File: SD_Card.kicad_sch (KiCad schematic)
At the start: 1 part, among them J8 Micro_SD_Card_Det1

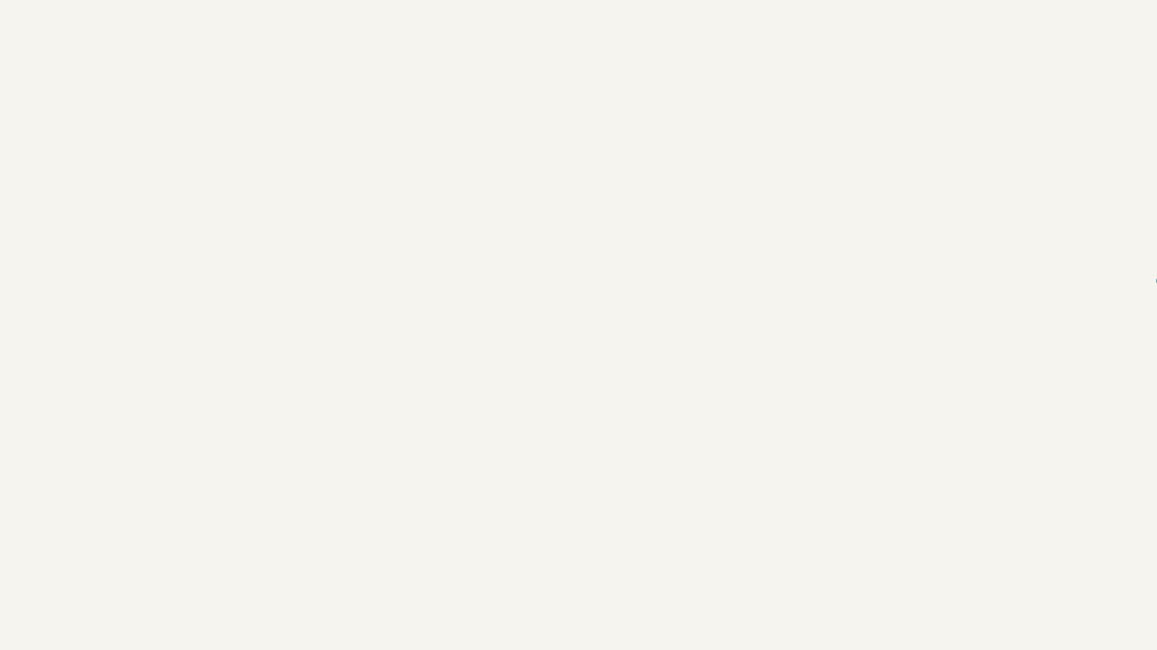
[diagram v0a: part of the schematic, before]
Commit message: Added SD card protection
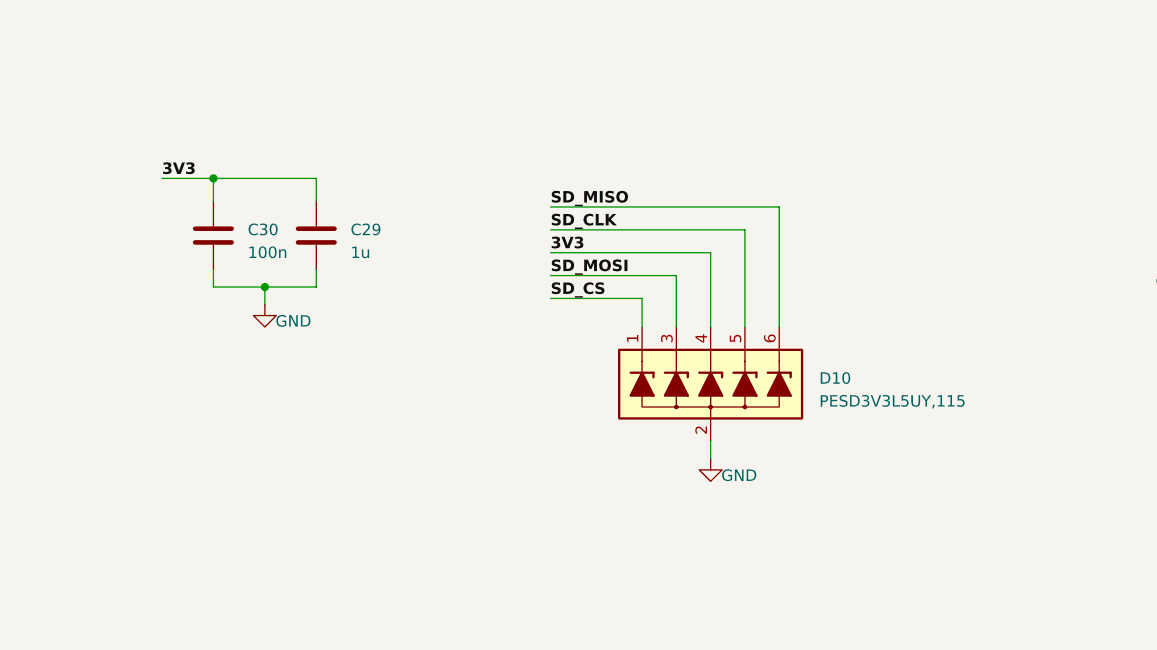
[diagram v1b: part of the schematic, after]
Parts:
- added C29: 1u, symbol ESP32-S3_DB:C
- added C30: 100n, symbol ESP32-S3_DB:C
- added D10: PESD3V3L5UY,115, Package_TO_SOT_SMD_AKL:SOT-363_SC-70-6, symbol ESP32-S3_DB:PESD3V3L5UY
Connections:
- net 3V3: now also C29.1, C30.1, D10.4 (L3)
- net GND: now also C29.2, C30.2, D10.2 (VN)
- net SD_CLK: now also D10.5 (L4)
- net SD_CS: now also D10.1 (L1)
- net SD_MISO: now also D10.6 (L5)
- net SD_MOSI: now also D10.3 (L2)
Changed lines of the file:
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@@
 (kicad_sch (version 20230121) (generator eeschema)
   (paper "A4")
+  (junction (at 80.645 70.485) (diameter 0) (color 0 0 0 0)
+  )
+  (junction (at 74.93 58.42) (diameter 0) (color 0 0 0 0)
+  )
   (no_connect (at 196.85 70.485))
   (no_connect (at 240.03 75.565))
@@
     (stroke (width 0) (type default))
   )
+  (wire (pts (xy 74.93 70.485) (xy 80.645 70.485))
+    (stroke (width 0) (type default))
+  )
   (wire (pts (xy 40.64 164.465) (xy 29.21 164.465))
     (stroke (width 0) (type default))
   )
+  (wire (pts (xy 112.395 69.215) (xy 126.365 69.215))
+    (stroke (width 0) (type default))
+  )
+  (wire (pts (xy 74.93 58.42) (xy 86.36 58.42))
+    (stroke (width 0) (type default))
+  )
+  (wire (pts (xy 86.36 70.485) (xy 86.36 68.58))
+    (stroke (width 0) (type default))
+  )
   (wire (pts (xy 40.64 167.005) (xy 29.21 167.005))
     (stroke (width 0) (type default))
   )
+  (wire (pts (xy 74.93 68.58) (xy 74.93 70.485))
+    (stroke (width 0) (type default))
+  )
   (wire (pts (xy 40.64 169.545) (xy 29.21 169.545))
     (stroke (width 0) (type default))
   )
+  (wire (pts (xy 130.175 66.675) (xy 130.175 74.93))
+    (stroke (width 0) (type default))
+  )
+  (wire (pts (xy 137.795 61.595) (xy 137.795 74.93))
+    (stroke (width 0) (type default))
+  )
   (wire (pts (xy 181.61 65.405) (xy 196.85 65.405))
     (stroke (width 0) (type default))
   )
+  (wire (pts (xy 74.93 60.96) (xy 74.93 58.42))
+    (stroke (width 0) (type default))
+  )
   (wire (pts (xy 184.15 55.245) (xy 196.85 55.245))
     (stroke (width 0) (type default))
   )
+  (wire (pts (xy 126.365 69.215) (xy 126.365 74.93))
+    (stroke (width 0) (type default))
+  )
+  (wire (pts (xy 80.645 70.485) (xy 86.36 70.485))
+    (stroke (width 0) (type default))
+  )
+  (wire (pts (xy 112.395 71.755) (xy 122.555 71.755))
+    (stroke (width 0) (type default))
+  )
+  (wire (pts (xy 80.645 70.485) (xy 80.645 72.39))
+    (stroke (width 0) (type default))
+  )
+  (wire (pts (xy 130.175 89.535) (xy 130.175 87.63))
+    (stroke (width 0) (type default))
+  )
+  (wire (pts (xy 112.395 66.675) (xy 130.175 66.675))
+    (stroke (width 0) (type default))
+  )
+  (wire (pts (xy 122.555 71.755) (xy 122.555 74.93))
+    (stroke (width 0) (type default))
+  )
   (wire (pts (xy 184.15 57.785) (xy 196.85 57.785))
     (stroke (width 0) (type default))
   )
+  (wire (pts (xy 112.395 64.135) (xy 133.985 64.135))
+    (stroke (width 0) (type default))
+  )
   (wire (pts (xy 184.15 62.865) (xy 196.85 62.865))
     (stroke (width 0) (type default))
   )
+  (wire (pts (xy 86.36 58.42) (xy 86.36 60.96))
+    (stroke (width 0) (type default))
+  )
+  (wire (pts (xy 112.395 61.595) (xy 137.795 61.595))
+    (stroke (width 0) (type default))
+  )
   (wire (pts (xy 40.64 174.625) (xy 29.21 174.625))
     (stroke (width 0) (type default))
   )
+  (wire (pts (xy 69.215 58.42) (xy 74.93 58.42))
+    (stroke (width 0) (type default))
+  )
   (wire (pts (xy 184.15 60.325) (xy 196.85 60.325))
     (stroke (width 0) (type default))
@@
     (stroke (width 0) (type default))
   )
+  (wire (pts (xy 133.985 64.135) (xy 133.985 74.93))
+    (stroke (width 0) (type default))
+  )
   (label "SD_CS" (at 184.15 55.245 0) (fields_autoplaced)
     (effects (font (size 1.27 1.27) bold (color 204 102 0 1)) (justify left bottom))
   )
+  (label "SD_CS" (at 112.395 71.755 0) (fields_autoplaced)
+    (effects (font (size 1.27 1.27) bold (color 204 102 0 1)) (justify left bottom))
+  )
   (label "SD_CLK" (at 40.64 169.545 0) (fields_autoplaced)
     (effects (font (size 1.27 1.27) bold (color 204 102 0 1)) (justify left bottom))
@@
     (effects (font (size 1.27 1.27) bold (color 204 102 0 1)) (justify left bottom))
   )
+  (label "3V3" (at 112.395 66.675 0) (fields_autoplaced)
+    (effects (font (size 1.27 1.27) bold (color 255 0 0 1)) (justify left bottom))
+  )
   (label "SD_MOSI" (at 184.15 57.785 0) (fields_autoplaced)
+    (effects (font (size 1.27 1.27) bold (color 204 102 0 1)) (justify left bottom))
+  )
+  (label "SD_MOSI" (at 112.395 69.215 0) (fields_autoplaced)
     (effects (font (size 1.27 1.27) bold (color 204 102 0 1)) (justify left bottom))
   )
@@
     (effects (font (size 1.27 1.27) bold (color 255 0 0 1)) (justify left bottom))
   )
+  (label "SD_MISO" (at 112.395 61.595 0) (fields_autoplaced)
+    (effects (font (size 1.27 1.27) bold (color 204 102 0 1)) (justify left bottom))
+  )
   (label "3V3" (at 184.15 60.325 0) (fields_autoplaced)
     (effects (font (size 1.27 1.27) bold (color 255 0 0 1)) (justify left bottom))
@@
   (label "SD_CS" (at 40.64 167.005 0) (fields_autoplaced)
     (effects (font (size 1.27 1.27) bold (color 204 102 0 1)) (justify left bottom))
+  )
+  (label "SD_CLK" (at 112.395 64.135 0) (fields_autoplaced)
+    (effects (font (size 1.27 1.27) bold (color 204 102 0 1)) (justify left bottom))
+  )
+  (label "3V3" (at 69.215 58.42 0) (fields_autoplaced)
+    (effects (font (size 1.27 1.27) bold (color 255 0 0 1)) (justify left bottom))
   )
   (label "SD_CLK" (at 184.15 62.865 0) (fields_autoplaced)
@@
         )
       )
+    )
+  )
+  (symbol (lib_id "ESP32-S3_DB:GND") (at 130.175 89.535 0) (unit 1)
+    (in_bom yes) (on_board yes) (dnp no)
+    (property "Reference" "#PWR055" (at 130.175 95.885 0)
+      (effects (font (size 1.27 1.27)) hide)
+    )
+    (property "Value" "GND" (at 133.35 91.44 0)
+      (effects (font (size 1.27 1.27)))
+    )
+    (property "Footprint" "" (at 130.175 89.535 0)
+      (effects (font (size 1.27 1.27)) hide)
+    )
+    (property "Datasheet" "" (at 130.175 89.535 0)
+      (effects (font (size 1.27 1.27)) hide)
+    )
+    (pin "1")
+    (instances
+      (project "ESP32-S3_DB"
+        (path "/b7fc4bd3-c219-4455-832b-8d795385dcf1/3994ddb3-4428-4f96-b9f4-a7790f668af6"
+          (reference "#PWR055") (unit 1)
+        )
+      )
+    )
+  )
+  (symbol (lib_id "ESP32-S3_DB:GND") (at 80.645 72.39 0) (unit 1)
+    (in_bom yes) (on_board yes) (dnp no)
+    (property "Reference" "#PWR056" (at 80.645 78.74 0)
+      (effects (font (size 1.27 1.27)) hide)
+    )
+    (property "Value" "GND" (at 83.82 74.295 0)
+      (effects (font (size 1.27 1.27)))
+    )
+    (property "Footprint" "" (at 80.645 72.39 0)
+      (effects (font (size 1.27 1.27)) hide)
+    )
+    (property "Datasheet" "" (at 80.645 72.39 0)
+      (effects (font (size 1.27 1.27)) hide)
+    )
+    (pin "1")
+    (instances
+      (project "ESP32-S3_DB"
+        (path "/b7fc4bd3-c219-4455-832b-8d795385dcf1/3994ddb3-4428-4f96-b9f4-a7790f668af6"
+          (reference "#PWR056") (unit 1)
+        )
+      )
+    )
+  )
+  (symbol (lib_id "ESP32-S3_DB:C") (at 74.93 64.77 0) (unit 1)
+    (in_bom yes) (on_board yes) (dnp no) (fields_autoplaced)
+    (property "Reference" "C30" (at 78.74 64.135 0)
+      (effects (font (size 1.27 1.27)) (justify left))
+    )
+    (property "Value" "100n" (at 78.74 66.675 0)
+      (effects (font (size 1.27 1.27)) (justify left))
+    )
+    (property "Footprint" "" (at 75.8952 68.58 0)
+      (effects (font (size 1.27 1.27)) hide)
+    )
+    (property "Datasheet" "~" (at 74.93 64.77 0)
+      (effects (font (size 1.27 1.27)) hide)
+    )
+    (pin "1")
+    (pin "2")
+    (instances
+      (project "ESP32-S3_DB"
+        (path "/b7fc4bd3-c219-4455-832b-8d795385dcf1/3994ddb3-4428-4f96-b9f4-a7790f668af6"
+          (reference "C30") (unit 1)
+        )
+      )
+    )
+  )
+  (symbol (lib_id "ESP32-S3_DB:C") (at 86.36 64.77 0) (unit 1)
+    (in_bom yes) (on_board yes) (dnp no) (fields_autoplaced)
+    (property "Reference" "C29" (at 90.17 64.135 0)
+      (effects (font (size 1.27 1.27)) (justify left))
+    )
+    (property "Value" "1u" (at 90.17 66.675 0)
+      (effects (font (size 1.27 1.27)) (justify left))
+    )
+    (property "Footprint" "" (at 87.3252 68.58 0)
+      (effects (font (size 1.27 1.27)) hide)
+    )
+    (property "Datasheet" "~" (at 86.36 64.77 0)
+      (effects (font (size 1.27 1.27)) hide)
+    )
+    (pin "1")
+    (pin "2")
+    (instances
+      (project "ESP32-S3_DB"
+        (path "/b7fc4bd3-c219-4455-832b-8d795385dcf1/3994ddb3-4428-4f96-b9f4-a7790f668af6"
+          (reference "C29") (unit 1)
+        )
+      )
+    )
+  )
+  (symbol (lib_id "ESP32-S3_DB:PESD3V3L5UY") (at 130.175 81.28 0) (unit 1)
+    (in_bom yes) (on_board yes) (dnp no) (fields_autoplaced)
+    (property "Reference" "D10" (at 142.24 80.645 0)
+      (effects (font (size 1.27 1.27)) (justify left))
+    )
+    (property "Value" "PESD3V3L5UY,115" (at 142.24 83.185 0)
+      (effects (font (size 1.27 1.27)) (justify left))
+    )
+    (property "Footprint" "Package_TO_SOT_SMD_AKL:SOT-363_SC-70-6" (at 130.175 81.28 0)
+      (effects (font (size 1.27 1.27)) hide)
+    )
+    (property "Datasheet" "https://www.tme.eu/Document/d7b061109274755b8c3532aab9d13eb5/PESD5V0L5UV-DTE.pdf" (at 130.175 81.28 0)
+      (effects (font (size 1.27 1.27)) hide)
+    )
+    (pin "1")
+    (pin "2")
+    (pin "3")
+    (pin "4")
+    (pin "5")
+    (pin "6")
+    (instances
+      (project "ESP32-S3_DB"
+        (path "/b7fc4bd3-c219-4455-832b-8d795385dcf1/3994ddb3-4428-4f96-b9f4-a7790f668af6"
+          (reference "D10") (unit 1)
+        )
+      )

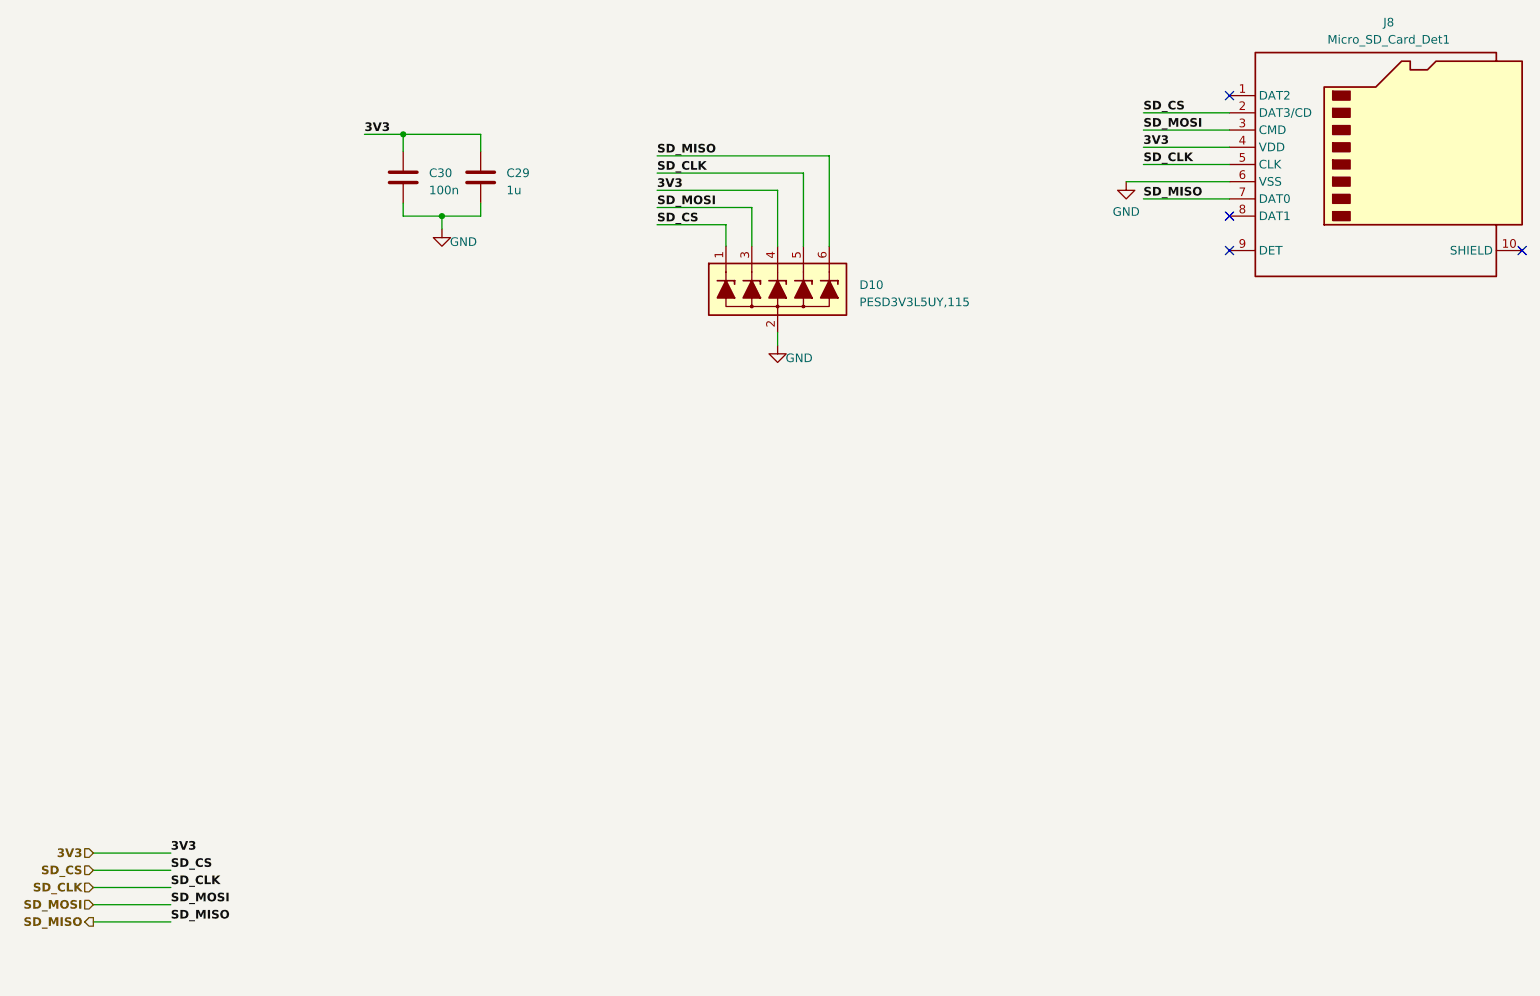
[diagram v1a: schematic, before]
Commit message: Added Female Headers
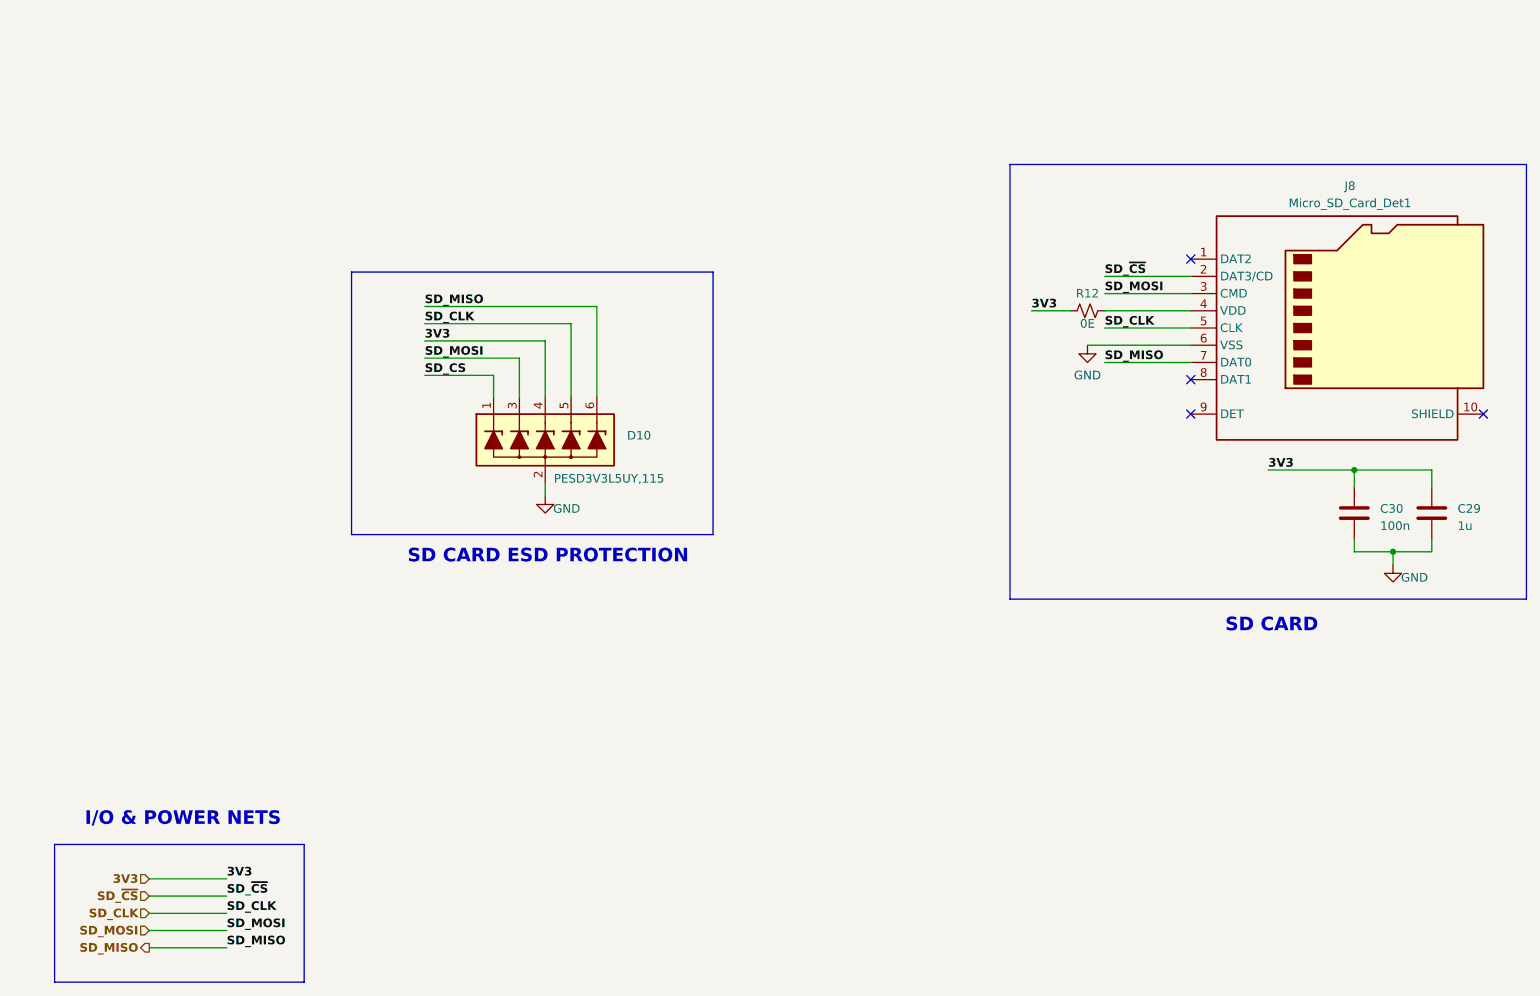
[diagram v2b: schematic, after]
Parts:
- added R12: 0E, symbol ESP32-S3_DB:R_Small_US
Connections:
- net 3V3: now also R12.1; no longer J8.4 (VDD)
- net SD_CS: no longer J8.2 (DAT3/CD)
- new net: J8.4 (VDD), R12.2
- new net SD_~{CS}: J8.2 (DAT3/CD)
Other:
- note added: "I/O & POWER NETS"
- note added: "SD CARD"
- note added: "SD CARD ESD PROTECTION"
- moved on the sheet: C29, C30, D10, J8

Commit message: Assigned PN and Footprint for C
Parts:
- C29: value 1u -> 1uF; footprint (none) -> ESP32-S3_DB:C_0603_1608Metric; PN (none) -> CC0603KRX5R8BB105
- C30: value 100n -> 100nF; footprint (none) -> ESP32-S3_DB:C_0402_1005Metric; PN (none) -> EMK107B7104KAHT
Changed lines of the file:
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@@
       (effects (font (size 1.27 1.27)) (justify left))
     )
-    (property "Value" "100n" (at 219.075 116.205 0)
+    (property "Value" "100nF" (at 219.075 116.205 0)
       (effects (font (size 1.27 1.27)) (justify left))
     )
-    (property "Footprint" "" (at 216.2302 118.11 0)
+    (property "Footprint" "ESP32-S3_DB:C_0402_1005Metric" (at 216.2302 118.11 0)
       (effects (font (size 1.27 1.27)) hide)
     )
     (property "Datasheet" "~" (at 215.265 114.3 0)
+      (effects (font (size 1.27 1.27)) hide)
+    )
+    (property "PN" "EMK107B7104KAHT" (at 215.265 114.3 0)
       (effects (font (size 1.27 1.27)) hide)
     )
@@
       (effects (font (size 1.27 1.27)) (justify left))
     )
-    (property "Value" "1u" (at 230.505 116.205 0)
+    (property "Value" "1uF" (at 230.505 116.205 0)
       (effects (font (size 1.27 1.27)) (justify left))
     )
-    (property "Footprint" "" (at 227.6602 118.11 0)
+    (property "Footprint" "ESP32-S3_DB:C_0603_1608Metric" (at 227.6602 118.11 0)
       (effects (font (size 1.27 1.27)) hide)
     )
@@
       (effects (font (size 1.27 1.27)) hide)
     )
+    (property "PN" "CC0603KRX5R8BB105" (at 226.695 114.3 0)
+      (effects (font (size 1.27 1.27)) hide)
+    )

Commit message: Assigned footprints
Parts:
- C29: footprint ESP32-S3_DB:C_0603_1608Metric -> ESP32-S3_Dev_Board:C_0603_1608Metric
- C30: footprint ESP32-S3_DB:C_0402_1005Metric -> ESP32-S3_Dev_Board:C_0402_1005Metric
- D10: footprint Package_TO_SOT_SMD_AKL:SOT-363_SC-70-6 -> ESP32-S3_Dev_Board:SOT-363_SC-70-6; PN (none) -> PESD2CAN
- R12: footprint (none) -> ESP32-S3_Dev_Board:R_0603_1608Metric; PN (none) -> RC0603JR-070RL
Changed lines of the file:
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@@
       (effects (font (size 1.27 1.27)))
     )
-    (property "Footprint" "" (at 175.895 84.455 0)
+    (property "Footprint" "ESP32-S3_Dev_Board:R_0603_1608Metric" (at 175.895 84.455 0)
       (effects (font (size 1.27 1.27)) hide)
     )
     (property "Datasheet" "~" (at 175.895 84.455 0)
+      (effects (font (size 1.27 1.27)) hide)
+    )
+    (property "PN" "RC0603JR-070RL" (at 175.895 84.455 0)
       (effects (font (size 1.27 1.27)) hide)
     )
@@
       (effects (font (size 1.27 1.27)) (justify left))
     )
-    (property "Footprint" "ESP32-S3_DB:C_0402_1005Metric" (at 216.2302 118.11 0)
+    (property "Footprint" "ESP32-S3_Dev_Board:C_0402_1005Metric" (at 216.2302 118.11 0)
       (effects (font (size 1.27 1.27)) hide)
     )
@@
       (effects (font (size 1.27 1.27)) (justify left))
     )
-    (property "Footprint" "ESP32-S3_DB:C_0603_1608Metric" (at 227.6602 118.11 0)
+    (property "Footprint" "ESP32-S3_Dev_Board:C_0603_1608Metric" (at 227.6602 118.11 0)
       (effects (font (size 1.27 1.27)) hide)
     )
@@
       (effects (font (size 1.27 1.27)) (justify left))
     )
-    (property "Footprint" "Package_TO_SOT_SMD_AKL:SOT-363_SC-70-6" (at 95.885 103.505 0)
+    (property "Footprint" "ESP32-S3_Dev_Board:SOT-363_SC-70-6" (at 95.885 103.505 0)
       (effects (font (size 1.27 1.27)) hide)
     )
@@
       (effects (font (size 1.27 1.27)) hide)
     )
+    (property "PN" "PESD2CAN" (at 95.885 103.505 0)
+      (effects (font (size 1.27 1.27)) hide)
+    )
